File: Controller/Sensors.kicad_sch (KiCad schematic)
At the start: 8 parts, among them J2 Conn_01x04, U2 BMI088, U3 MMC5983MA

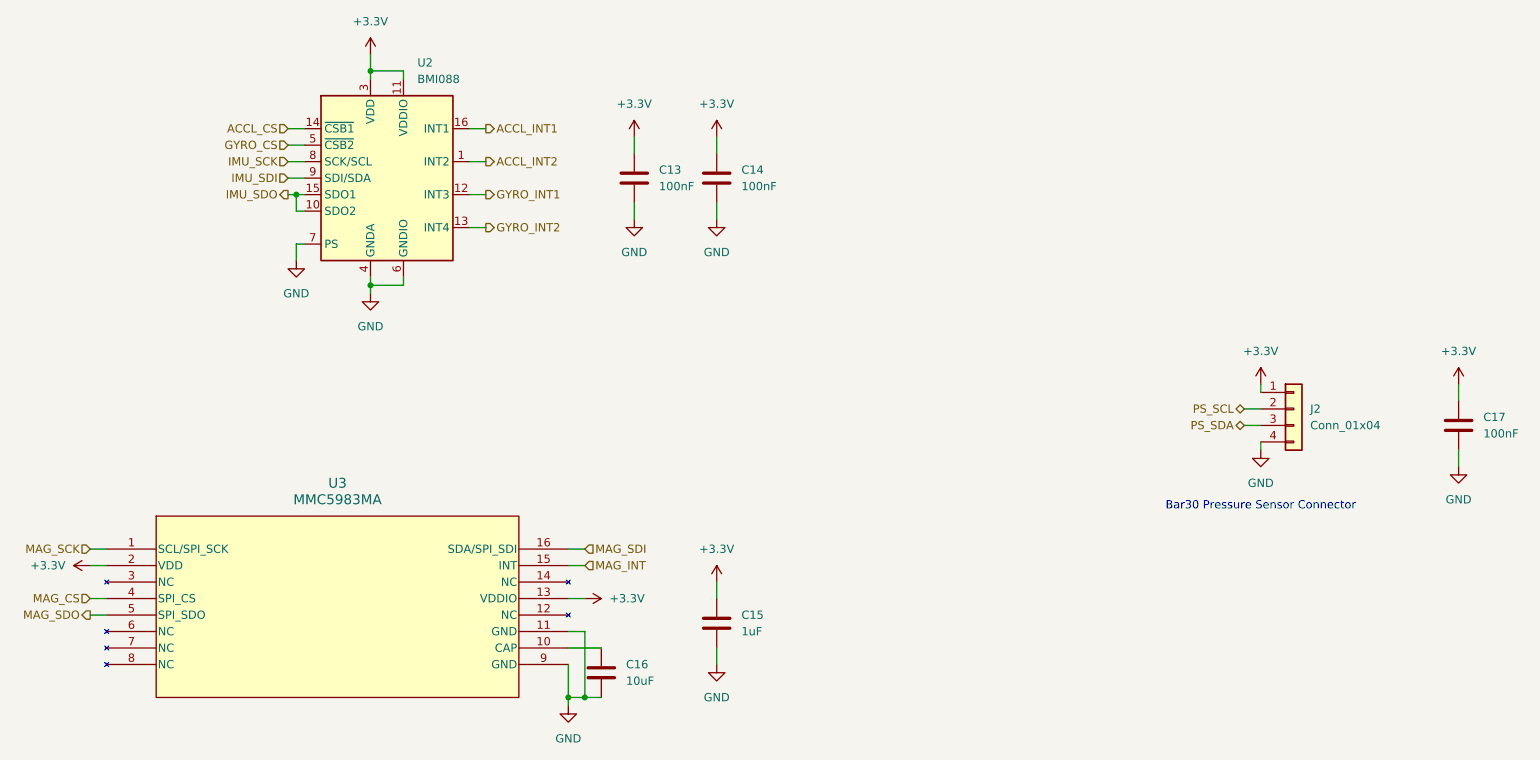
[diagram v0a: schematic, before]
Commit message: Reorganize controller schematic
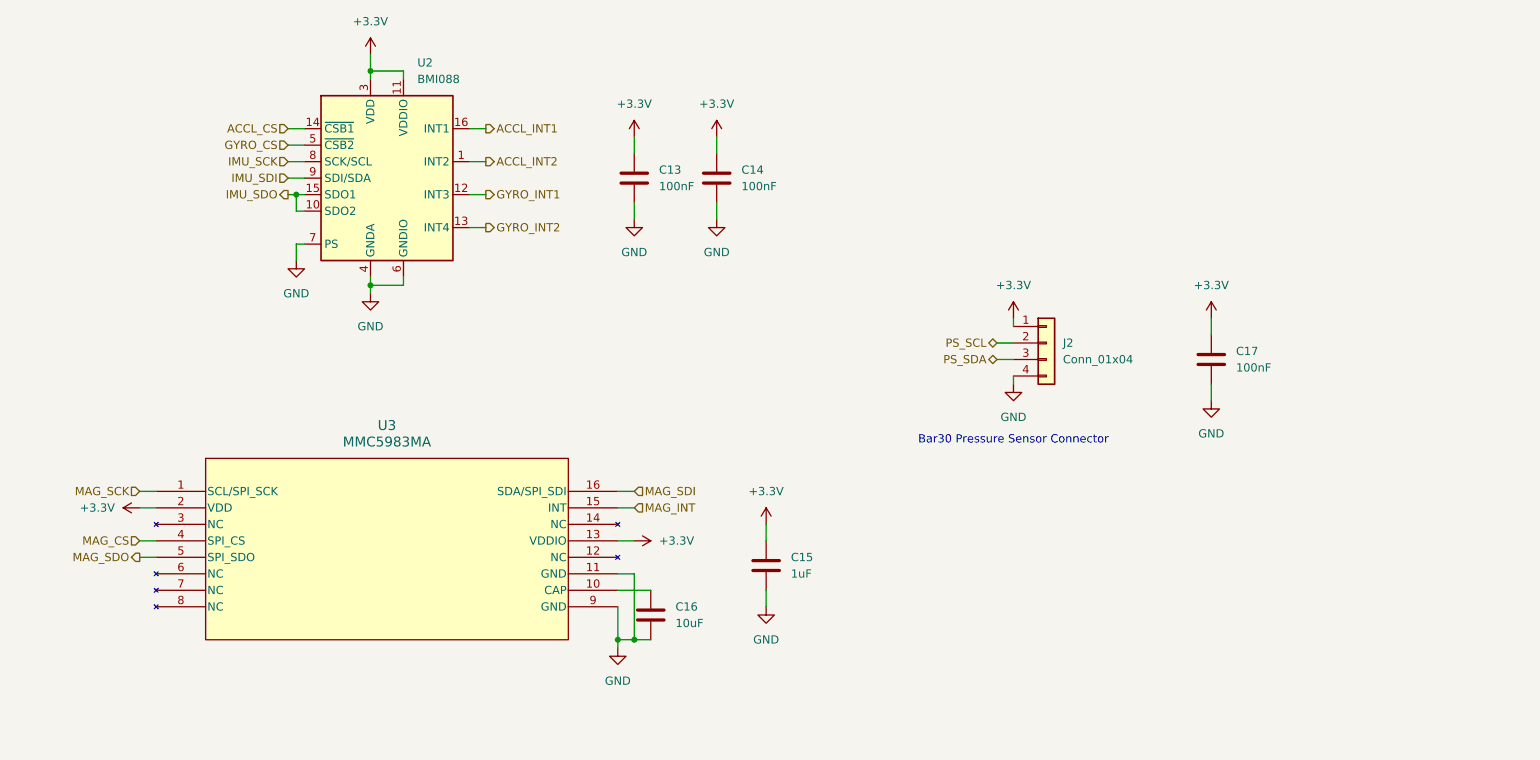
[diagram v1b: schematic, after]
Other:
- moved on the sheet: C15, C16, C17, J2, U3

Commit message: Re-number components in controller schematic
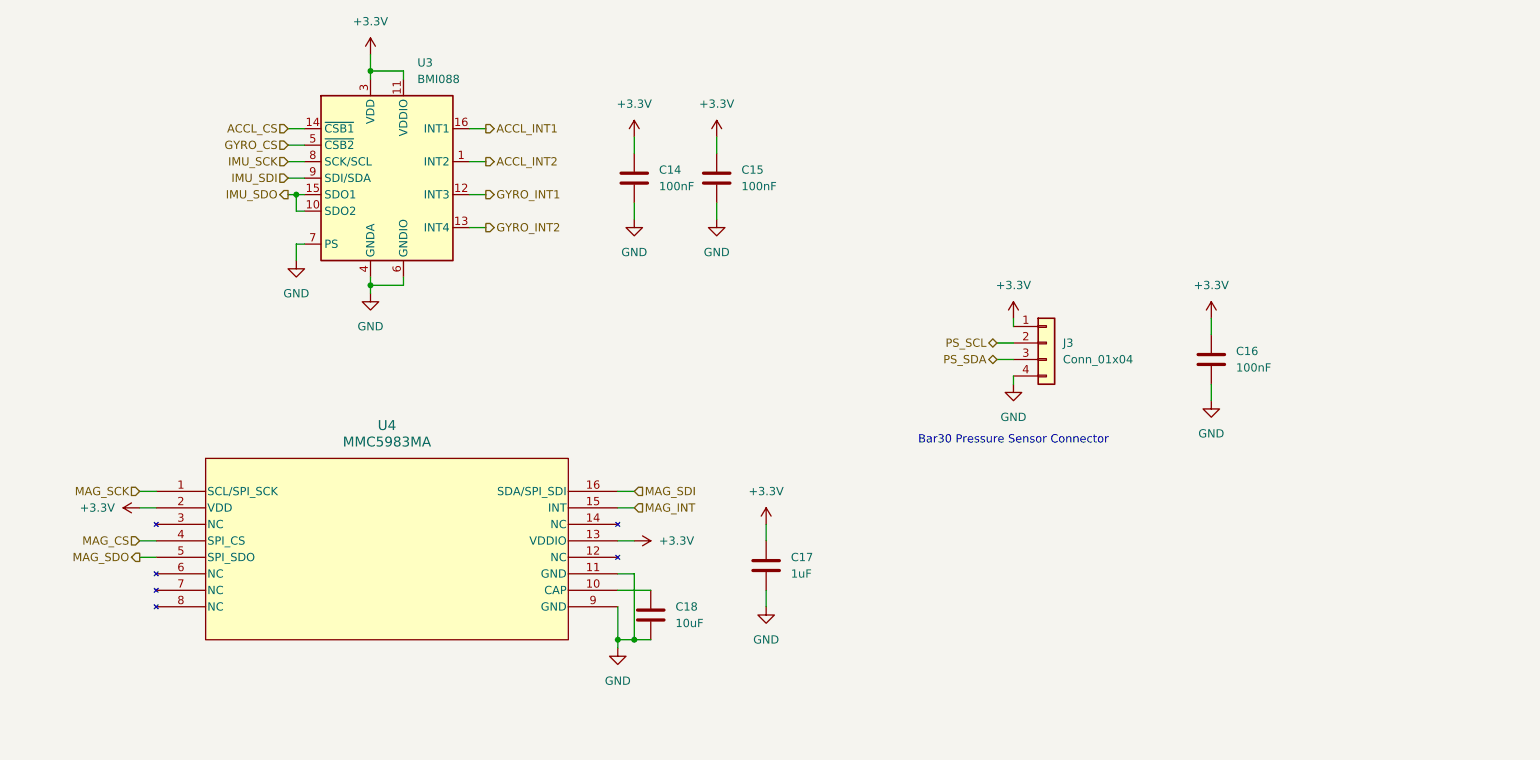
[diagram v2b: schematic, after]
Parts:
- renumbered C13 to C14, C14 to C15, C17 to C16, C15 to C17, C16 to C18, J2 to J3, U2 to U3, U3 to U4
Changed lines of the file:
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@@
 		(dnp no)
 		(fields_autoplaced yes)
-		(property "Reference" "#PWR027"
+		(property "Reference" "#PWR035"
 			(at 147.32 107.95 0)
 			(effects
@@
 			(project "XuLabController"
 				(path "/71bb14ae-b730-4d22-a41d-cf68989dae2d/a5713b00-422c-456a-9938-13721b057665"
-					(reference "#PWR027")
+					(reference "#PWR035")
 					(unit 1)
 				)
@@
 		(dnp no)
 		(fields_autoplaced yes)
-		(property "Reference" "#PWR036"
+		(property "Reference" "#PWR031"
 			(at 215.9 76.2 0)
 			(effects
@@
 			(project "XuLabController"
 				(path "/71bb14ae-b730-4d22-a41d-cf68989dae2d/a5713b00-422c-456a-9938-13721b057665"
-					(reference "#PWR036")
+					(reference "#PWR031")
 					(unit 1)
 				)
@@
 		(dnp no)
 		(fields_autoplaced yes)
-		(property "Reference" "#PWR035"
+		(property "Reference" "#PWR027"
 			(at 139.7 63.5 0)
 			(effects
@@
 			(project "XuLabController"
 				(path "/71bb14ae-b730-4d22-a41d-cf68989dae2d/a5713b00-422c-456a-9938-13721b057665"
-					(reference "#PWR035")
+					(reference "#PWR027")
 					(unit 1)
 				)
@@
 		(dnp no)
 		(fields_autoplaced yes)
-		(property "Reference" "#PWR034"
+		(property "Reference" "#PWR024"
 			(at 127 48.26 0)
 			(effects
@@
 			(project "XuLabController"
 				(path "/71bb14ae-b730-4d22-a41d-cf68989dae2d/a5713b00-422c-456a-9938-13721b057665"
-					(reference "#PWR034")
+					(reference "#PWR024")
 					(unit 1)
 				)
@@
 		(on_board yes)
 		(dnp no)
-		(property "Reference" "J2"
+		(property "Reference" "J3"
 			(at 193.04 76.1999 0)
 			(effects
@@
 			(project "XuLabController"
 				(path "/71bb14ae-b730-4d22-a41d-cf68989dae2d/a5713b00-422c-456a-9938-13721b057665"
-					(reference "J2")
+					(reference "J3")
 					(unit 1)
 				)
@@
 		(dnp no)
 		(fields_autoplaced yes)
-		(property "Reference" "C15"
+		(property "Reference" "C17"
 			(at 151.13 109.2199 0)
 			(effects
@@
 			(project "XuLabController"
 				(path "/71bb14ae-b730-4d22-a41d-cf68989dae2d/a5713b00-422c-456a-9938-13721b057665"
-					(reference "C15")
+					(reference "C17")
 					(unit 1)
 				)
@@
 		(dnp no)
 		(fields_autoplaced yes)
-		(property "Reference" "#PWR051"
+		(property "Reference" "#PWR033"
 			(at 215.9 91.44 0)
 			(effects
@@
 			(project "XuLabController"
 				(path "/71bb14ae-b730-4d22-a41d-cf68989dae2d/a5713b00-422c-456a-9938-13721b057665"
-					(reference "#PWR051")
+					(reference "#PWR033")
 					(unit 1)
 				)
@@
 		(dnp no)
 		(fields_autoplaced yes)
-		(property "Reference" "#PWR037"
+		(property "Reference" "#PWR034"
 			(at 54.61 101.6 0)
 			(effects
@@
 			(project "XuLabController"
 				(path "/71bb14ae-b730-4d22-a41d-cf68989dae2d/a5713b00-422c-456a-9938-13721b057665"
-					(reference "#PWR037")
+					(reference "#PWR034")
 					(unit 1)
 				)
@@
 		(dnp no)
 		(fields_autoplaced yes)
-		(property "Reference" "U3"
+		(property "Reference" "U4"
 			(at 88.9 88.9 0)
 			(effects
@@
 			(project "XuLabController"
 				(path "/71bb14ae-b730-4d22-a41d-cf68989dae2d/a5713b00-422c-456a-9938-13721b057665"
-					(reference "U3")
+					(reference "U4")
 					(unit 1)
 				)
@@
 		(dnp no)
 		(fields_autoplaced yes)
-		(property "Reference" "#PWR030"
+		(property "Reference" "#PWR025"
 			(at 139.7 48.26 0)
 			(effects
@@
 			(project "XuLabController"
 				(path "/71bb14ae-b730-4d22-a41d-cf68989dae2d/a5713b00-422c-456a-9938-13721b057665"
-					(reference "#PWR030")
+					(reference "#PWR025")
 					(unit 1)
 				)
@@
 		(dnp no)
 		(fields_autoplaced yes)
-		(property "Reference" "#PWR025"
+		(property "Reference" "#PWR038"
 			(at 124.46 129.54 0)
 			(effects
@@
 			(project "XuLabController"
 				(path "/71bb14ae-b730-4d22-a41d-cf68989dae2d/a5713b00-422c-456a-9938-13721b057665"
-					(reference "#PWR025")
+					(reference "#PWR038")
 					(unit 1)
 				)
@@
 		(dnp no)
 		(fields_autoplaced yes)
-		(property "Reference" "C13"
+		(property "Reference" "C14"
 			(at 130.81 49.5299 0)
 			(effects
@@
 			(project "XuLabController"
 				(path "/71bb14ae-b730-4d22-a41d-cf68989dae2d/a5713b00-422c-456a-9938-13721b057665"
-					(reference "C13")
+					(reference "C14")
 					(unit 1)
 				)
@@
 		(on_board yes)
 		(dnp no)
-		(property "Reference" "#PWR050"
+		(property "Reference" "#PWR032"
 			(at 185.42 88.9 0)
 			(effects
@@
 			(project "XuLabController"
 				(path "/71bb14ae-b730-4d22-a41d-cf68989dae2d/a5713b00-422c-456a-9938-13721b057665"
-					(reference "#PWR050")
+					(reference "#PWR032")
 					(unit 1)
 				)
@@
 		(dnp no)
 		(fields_autoplaced yes)
-		(property "Reference" "#PWR033"
+		(property "Reference" "#PWR030"
 			(at 185.42 76.2 0)
 			(effects
@@
 			(project "XuLabController"
 				(path "/71bb14ae-b730-4d22-a41d-cf68989dae2d/a5713b00-422c-456a-9938-13721b057665"
-					(reference "#PWR033")
+					(reference "#PWR030")
 					(unit 1)
 				)
@@
 		(dnp no)
 		(fields_autoplaced yes)
-		(property "Reference" "C17"
+		(property "Reference" "C16"
 			(at 219.71 77.4699 0)
 			(effects
@@
 			(project "XuLabController"
 				(path "/71bb14ae-b730-4d22-a41d-cf68989dae2d/a5713b00-422c-456a-9938-13721b057665"
-					(reference "C17")
+					(reference "C16")
 					(unit 1)
 				)
@@
 		(dnp no)
 		(fields_autoplaced yes)
-		(property "Reference" "C16"
+		(property "Reference" "C18"
 			(at 133.35 116.8399 0)
 			(effects
@@
 			(project "XuLabController"
 				(path "/71bb14ae-b730-4d22-a41d-cf68989dae2d/a5713b00-422c-456a-9938-13721b057665"
-					(reference "C16")
+					(reference "C18")
 					(unit 1)
 				)
@@
 		(dnp no)
 		(fields_autoplaced yes)
-		(property "Reference" "#PWR09"
+		(property "Reference" "#PWR029"
 			(at 86.36 74.93 0)
 			(effects
@@
 			(project "XuLabController"
 				(path "/71bb14ae-b730-4d22-a41d-cf68989dae2d/a5713b00-422c-456a-9938-13721b057665"
-					(reference "#PWR09")
+					(reference "#PWR029")
 					(unit 1)
 				)
@@
 		(dnp no)
 		(fields_autoplaced yes)
-		(property "Reference" "U2"
+		(property "Reference" "U3"
 			(at 93.5833 33.02 0)
 			(effects
@@
 			(project "XuLabController"
 				(path "/71bb14ae-b730-4d22-a41d-cf68989dae2d/a5713b00-422c-456a-9938-13721b057665"
-					(reference "U2")
+					(reference "U3")
 					(unit 1)
 				)
@@
 		(dnp no)
 		(fields_autoplaced yes)
-		(property "Reference" "#PWR08"
+		(property "Reference" "#PWR023"
 			(at 86.36 35.56 0)
 			(effects
@@
 			(project "XuLabController"
 				(path "/71bb14ae-b730-4d22-a41d-cf68989dae2d/a5713b00-422c-456a-9938-13721b057665"
-					(reference "#PWR08")
+					(reference "#PWR023")
 					(unit 1)
 				)
@@
 		(dnp no)
 		(fields_autoplaced yes)
-		(property "Reference" "#PWR028"
+		(property "Reference" "#PWR037"
 			(at 147.32 123.19 0)
 			(effects
@@
 			(project "XuLabController"
 				(path "/71bb14ae-b730-4d22-a41d-cf68989dae2d/a5713b00-422c-456a-9938-13721b057665"
-					(reference "#PWR028")
+					(reference "#PWR037")
 					(unit 1)
 				)
@@
 		(dnp no)
 		(fields_autoplaced yes)
-		(property "Reference" "C14"
+		(property "Reference" "C15"
 			(at 143.51 49.5299 0)
 			(effects
@@
 			(project "XuLabController"
 				(path "/71bb14ae-b730-4d22-a41d-cf68989dae2d/a5713b00-422c-456a-9938-13721b057665"
-					(reference "C14")
+					(reference "C15")
 					(unit 1)
 				)
@@
 		(dnp no)
 		(fields_autoplaced yes)
-		(property "Reference" "#PWR032"
+		(property "Reference" "#PWR026"
 			(at 127 63.5 0)
 			(effects
@@
 			(project "XuLabController"
 				(path "/71bb14ae-b730-4d22-a41d-cf68989dae2d/a5713b00-422c-456a-9938-13721b057665"
-					(reference "#PWR032")
+					(reference "#PWR026")
 					(unit 1)
 				)
@@
 		(dnp no)
 		(fields_autoplaced yes)
-		(property "Reference" "#PWR010"
+		(property "Reference" "#PWR028"
 			(at 74.93 69.85 0)
 			(effects
@@
 			(project "XuLabController"
 				(path "/71bb14ae-b730-4d22-a41d-cf68989dae2d/a5713b00-422c-456a-9938-13721b057665"
-					(reference "#PWR010")
+					(reference "#PWR028")
 					(unit 1)
 				)
@@
 		(dnp no)
 		(fields_autoplaced yes)
-		(property "Reference" "#PWR026"
+		(property "Reference" "#PWR036"
 			(at 123.19 106.68 0)
 			(effects
@@
 			(project "XuLabController"
 				(path "/71bb14ae-b730-4d22-a41d-cf68989dae2d/a5713b00-422c-456a-9938-13721b057665"
-					(reference "#PWR026")
-					(unit 1)
-				)
+					(reference "#PWR036")
+					(unit 1)
+				)
